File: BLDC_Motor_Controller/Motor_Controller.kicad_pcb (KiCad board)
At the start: 2 copper layers, 73 x 70 mm, 56 parts, among them J1 I/O, J2 PowerTab, J3 PowerTab, J4 PowerTab, J5 PowerTab, J6 PowerTab, J7 PowerTab, Q1 FDD86250-F085‎, Q2 FDD86250-F085‎, Q3 FDD86250-F085‎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

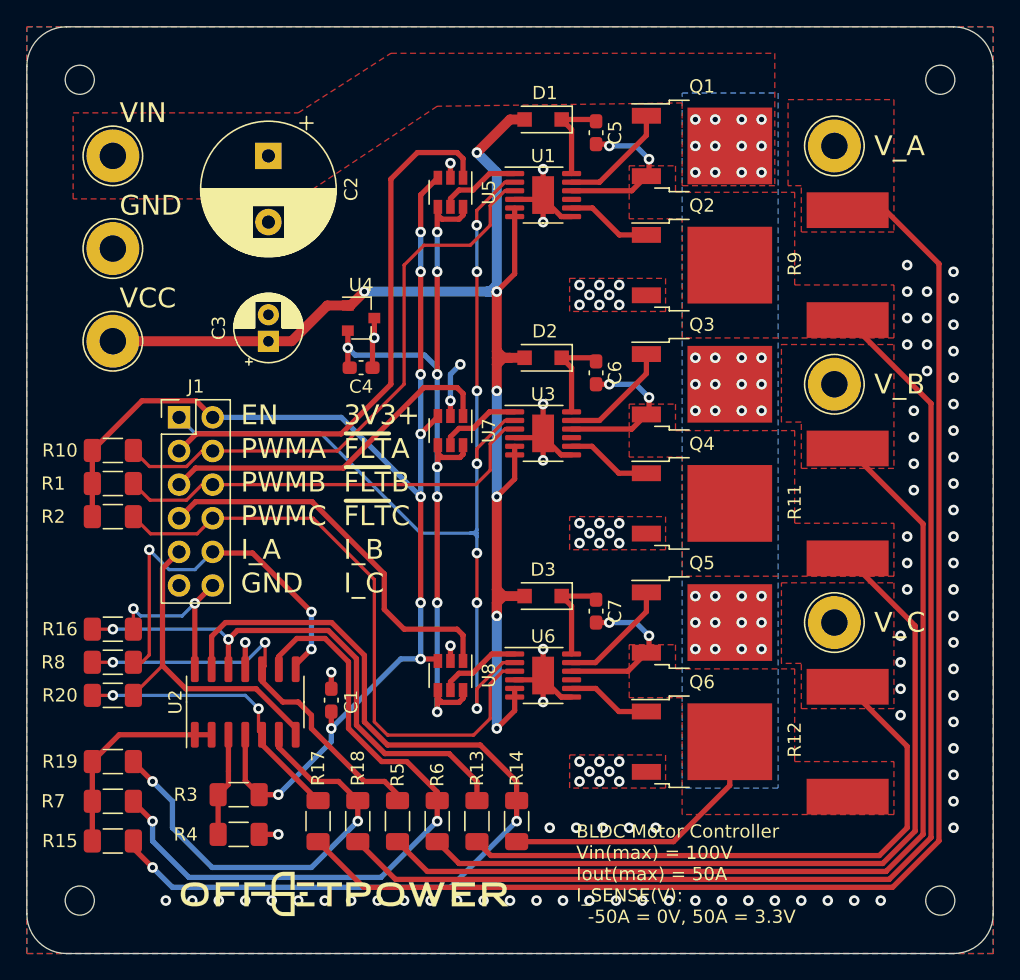
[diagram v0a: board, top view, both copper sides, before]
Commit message: Updated design
Added outputs with BOM
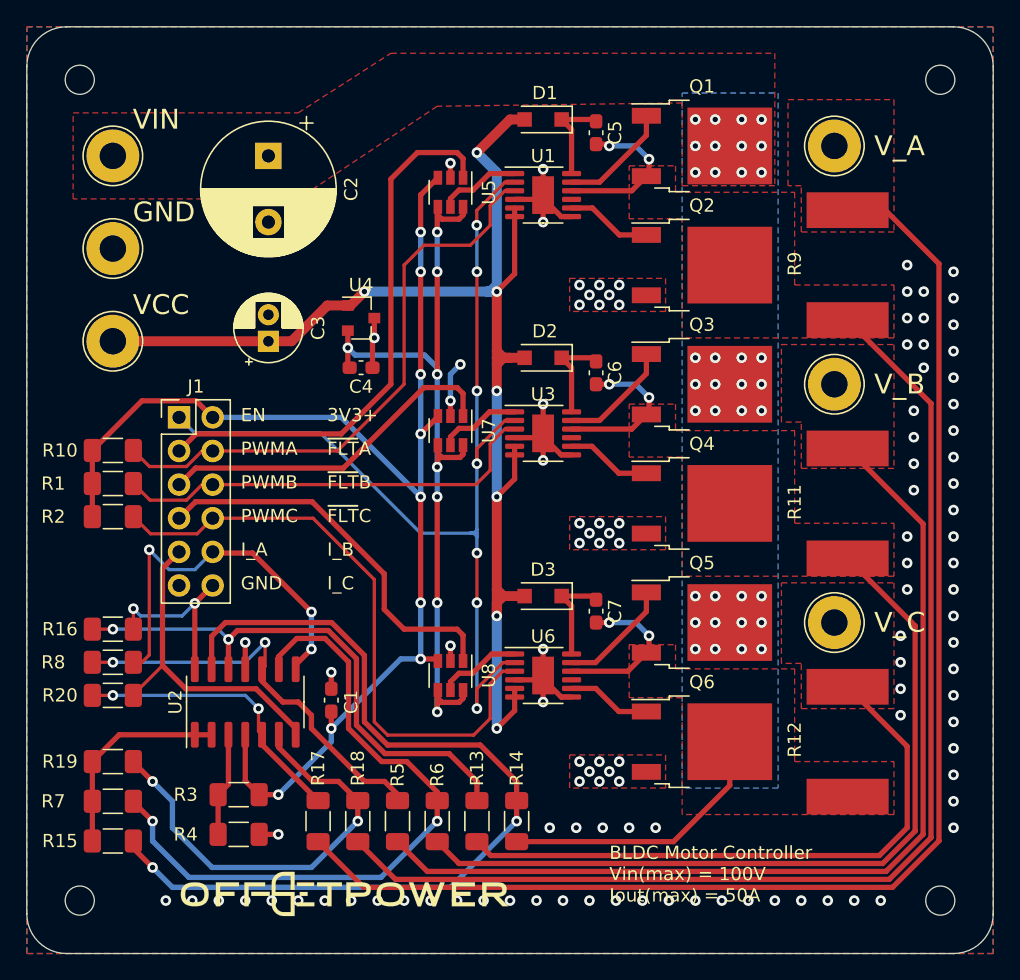
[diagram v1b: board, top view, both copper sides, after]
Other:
- board text added: "BLDC Motor Controller Vin(max) = 100V Iout(max) = 50A"
- board text removed: "BLDC Motor Controller Vin(max) = 100V Iout(max) = 50A I_SENSE(V): -50A = 0V, 50A = 3.3V"
